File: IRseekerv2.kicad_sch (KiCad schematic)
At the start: 39 parts, among them J1 Conn_01x01_Female, J10 Conn_01x01_Female, J11 Conn_01x01_Female, J12 Conn_01x01_Female, J13 RESET, J14 COMM, J15 SEL_VOLTAGE, J16 G, J17 G, J18 G, J19 G, J2 Conn_01x01_Female, J20 COMM, J21 Conn_01x01_Female, J22 Conn_01x01_Female, J23 Conn_01x01_Female, J24 Conn_01x01_Female, J3 Conn_01x01_Female, J4 Conn_01x01_Female, J5 Conn_01x01_Female, J6 Conn_01x01_Female, J7 Conn_01x01_Female, J8 Conn_01x01_Female, J9 Conn_01x01_Female, U1 WeAct-STM32G431CoreBoard, U10 TSSP58038, U11 TSSP58038, U12 TSSP58038, U13 TSSP58038, U14 TSSP58038, U15 TSSP58038, U16 TSSP58038, U2 CD4072B, U4 CD4072B, U5 TSSP58038, U6 TSSP58038, U7 TSSP58038, U8 TSSP58038, U9 TSSP58038

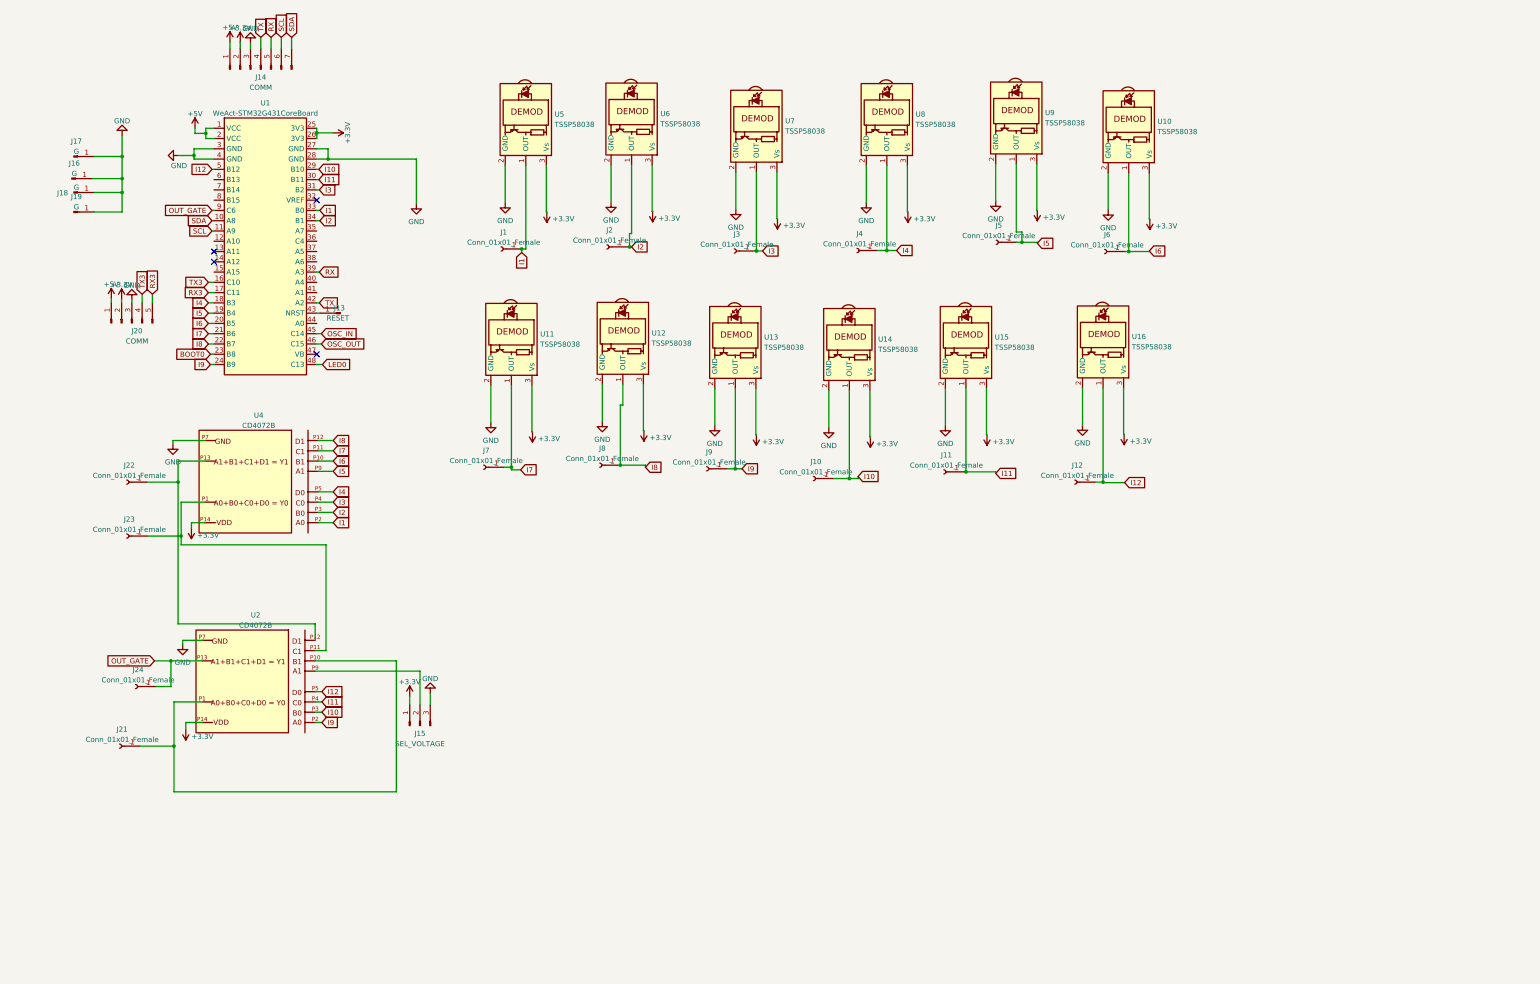
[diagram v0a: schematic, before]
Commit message: reworked to put STM32G431CBU6 on board
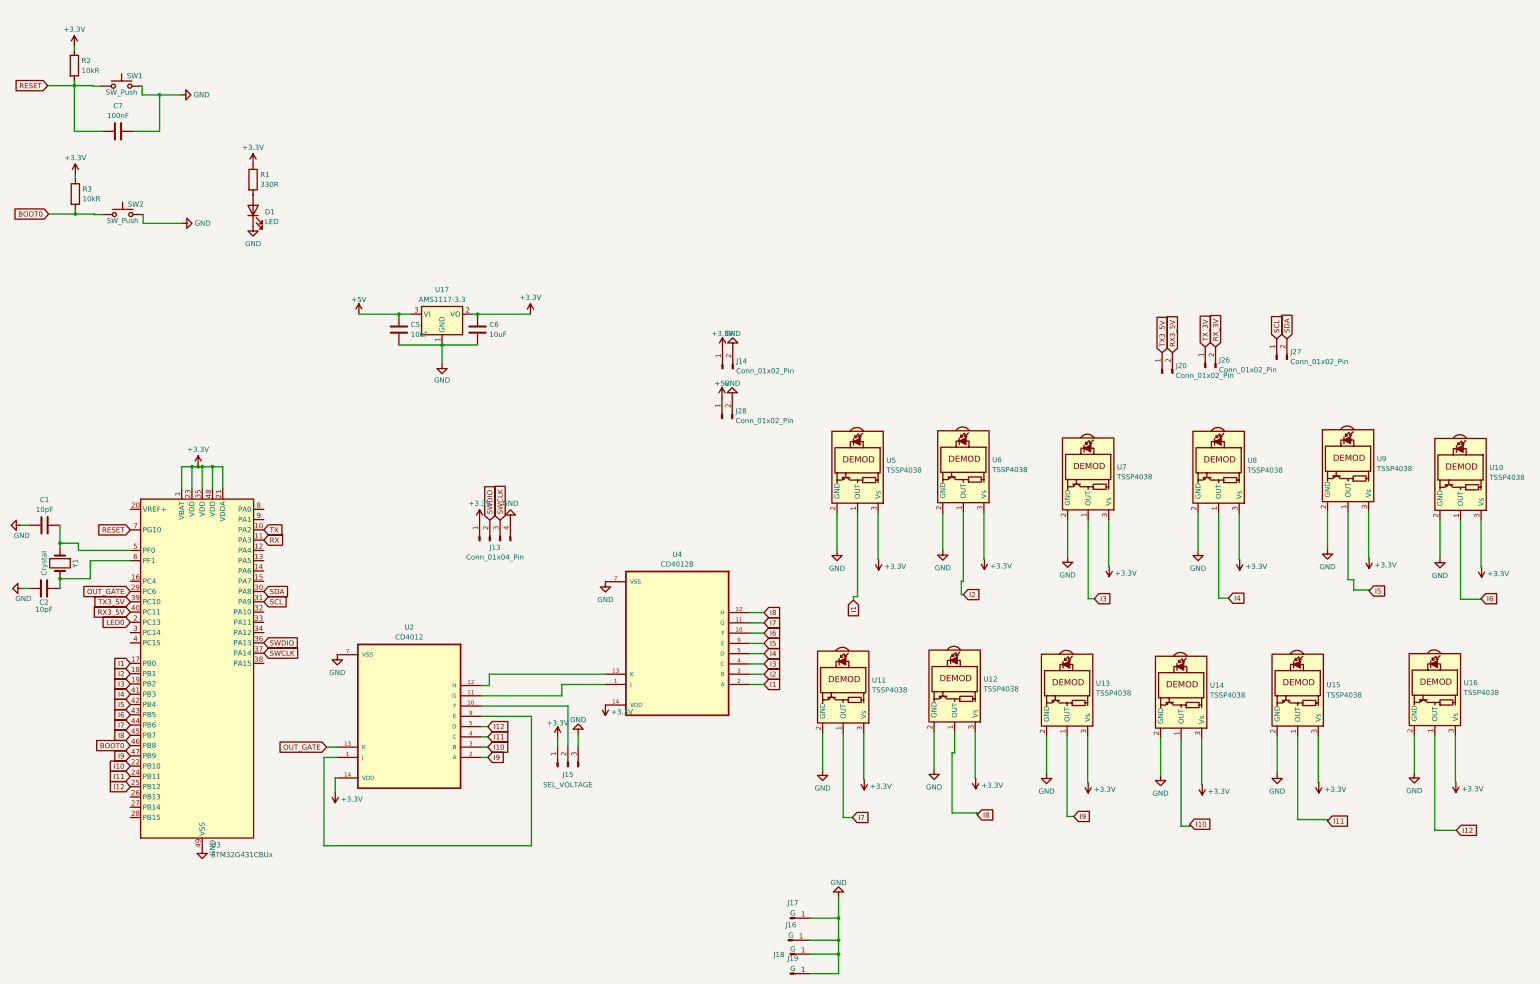
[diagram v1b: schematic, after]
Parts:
- removed J1, J10, J11, J12, J2, J21, J22, J23, J24, J3, J4, J5, J6, J7, J8, J9: Conn_01x01_Female, Connector_PinHeader_2.54mm:PinHeader_1x01_P2.54mm_Vertical, symbol Connector:Conn_01x01_Female
- removed J13: RESET, Connector_PinHeader_2.54mm:PinHeader_1x01_P2.54mm_Vertical, symbol Connector:Conn_01x01_Male
- removed J14: COMM, Connector_PinHeader_2.54mm:PinHeader_1x07_P2.54mm_Vertical, symbol Connector:Conn_01x07_Male
- removed J20: COMM, Connector_PinHeader_2.54mm:PinHeader_1x05_P2.54mm_Vertical, symbol Connector:Conn_01x05_Male
- removed U1: WeAct-STM32G431CoreBoard, bluepill:WeAct-STM32G431CoreBoard_MCU_Module, symbol bluepill:WeAct-STM32G431CoreBoard
- added C1, C2: 10pF, Capacitor_THT:C_Disc_D3.0mm_W1.6mm_P2.50mm, symbol Device:C
- added C5, C6: 10uF, Capacitor_THT:C_Disc_D3.0mm_W1.6mm_P2.50mm, symbol Device:C
- added C7: 100nF, Capacitor_THT:C_Disc_D3.0mm_W1.6mm_P2.50mm, symbol Device:C
- added D1: LED, LED_THT:LED_D3.0mm, symbol Device:LED
- added J13: Conn_01x04_Pin, Connector_PinHeader_2.54mm:PinHeader_1x04_P2.54mm_Vertical, symbol Connector:Conn_01x04_Pin
- added J14, J20, J26, J27, J28: Conn_01x02_Pin, Connector_PinHeader_2.54mm:PinHeader_1x02_P2.54mm_Vertical, symbol Connector:Conn_01x02_Pin
- added R1: 330R, Resistor_THT:R_Axial_DIN0204_L3.6mm_D1.6mm_P1.90mm_Vertical, symbol Device:R
- added R2, R3: 10kR, Resistor_THT:R_Axial_DIN0204_L3.6mm_D1.6mm_P1.90mm_Vertical, symbol Device:R
- added SW1, SW2: SW_Push, Button_Switch_THT:SW_PUSH_6mm, symbol Switch:SW_Push
- added U17: AMS1117-3.3, Package_TO_SOT_SMD:SOT-223-3_TabPin2, symbol Regulator_Linear:AMS1117-3.3
- added U3: STM32G431CBUx, Package_DFN_QFN:QFN-48-1EP_7x7mm_P0.5mm_EP5.6x5.6mm, symbol MCU_ST_STM32G4:STM32G431CBUx
- added Y1: Crystal, Crystal:Crystal_HC49-4H_Vertical, symbol Device:Crystal
- U10, U12, U14, U15, U5, U7: value TSSP58038 -> TSSP4038; footprint OptoDevice:Vishay_MINICAST-3Pin -> Vishay:Vishay_MINICAST-3Pin
- U11, U13, U16, U6, U8, U9: value TSSP58038 -> TSSP4038; footprint Library:Vishay_MINICAST-3PinMarek -> Vishay:Vishay_MINICAST-3Pin
- U2: value CD4072B -> CD4012; footprint CD4072B:DIP794W45P254L1969H508Q14 -> CD70xx:DIP794W45P254L1969H508Q14; symbol CD4072B:CD4072B -> CD4012:CD4012BE; Availability (none) -> In Stock; Check_prices (none) -> https://www.snapeda.com/parts/CD4012BE/Texas+Instruments/vi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; MF (none) -> Texas Instruments; MP (none) -> CD4012BE; Package (none) -> PDIP-14 Texas Instruments; Price (none) -> None; Purchase-URL (none) -> https://www.snapeda.com/api/url_track_click_mouser/?unipart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; SnapEDA_Link (none) -> https://www.snapeda.com/parts/CD4012BE/Texas+Instruments/vi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
- U4: value CD4072B -> CD4012B; footprint CD4072B:DIP794W45P254L1969H508Q14 -> CD70xx:DIP794W45P254L1969H508Q14; symbol CD4072B:CD4072B -> CD4012:CD4012BE; Availability (none) -> In Stock; Check_prices (none) -> https://www.snapeda.com/parts/CD4012BE/Texas+Instruments/vi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; MF (none) -> Texas Instruments; MP (none) -> CD4012BE; Package (none) -> PDIP-14 Texas Instruments; Price (none) -> None; Purchase-URL (none) -> https://www.snapeda.com/api/url_track_click_mouser/?unipart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; SnapEDA_Link (none) -> https://www.snapeda.com/parts/CD4012BE/Texas+Instruments/vi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
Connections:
- net +3.3V: now also U2.14 (VDD), U4.14 (VDD), C6.2, J13.1 (Pin_1), J14.1 (Pin_1), R1.1, R2.1, R3.1, U17.2 (VO), U3.1 (VBAT), U3.21 (VDDA), U3.23 (VDD), U3.35 (VDD), U3.48 (VDD); no longer U2.P14, U4.P14
- net +5V: now also C5.2, J28.1 (Pin_1), U17.3 (VI)
- net BOOT0: now also R3.2, SW2.1, U3.46 (PB8)
- net GND: now also U2.7 (VSS), U4.7 (VSS), C1.1, C2.1, C5.1, C6.1, C7.1, D1.1 (K), J13.4 (Pin_4), J14.2 (Pin_2), J28.2 (Pin_2), SW1.2, SW2.2, U17.1 (GND), U3.49 (VSS); no longer U2.P7, U4.P7
- net I1: now also U4.2 (A), U3.17 (PB0); no longer U4.P2
- net I10: now also U2.3 (B), U3.22 (PB10); no longer U2.P3
- net I11: now also U2.4 (C), U3.24 (PB11); no longer U2.P4
- net I12: now also U2.5 (D), U3.25 (PB12); no longer U2.P5
- net I2: now also U4.3 (B), U3.18 (PB1); no longer U4.P3
- net I3: now also U4.4 (C), U3.19 (PB2); no longer U4.P4
- net I4: now also U4.5 (D), U3.41 (PB3); no longer U4.P5
- net I5: now also U4.9 (E), U3.42 (PB4); no longer U4.P9
- net I6: now also U4.10 (F), U3.43 (PB5); no longer U4.P10
- net I7: now also U4.11 (G), U3.44 (PB6); no longer U4.P11
- net I8: now also U4.12 (H), U3.45 (PB7); no longer U4.P12
- net I9: now also U2.2 (A), U3.47 (PB9); no longer U2.P2
- net LED0: now also U3.2 (PC13)
- net OUT_GATE: now also U2.13 (K), U3.29 (PC6); no longer U2.P13
- net RX: now also U3.11 (PA3)
- net SCL: now also J27.1 (Pin_1), U3.31 (PA9)
- net SDA: now also J27.2 (Pin_2), U3.30 (PA8)
- net TX: now also U3.10 (PA2)
- net at J15.2 (Pin_2): now also U2.10 (F); no longer U2.P9
- new net: C2.2, U3.6 (PF1), Y1.2
- new net: C1.2, U3.5 (PF0), Y1.1
- new net: U2.11 (G), U4.1 (J)
- new net: U2.12 (H), U4.13 (K)
- new net: U2.1 (J), U2.9 (E)
- new net: D1.2 (A), R1.2
- new net RESET: C7.2, R2.2, SW1.1, U3.7 (PG10)
- new net RX3_5V: J20.2 (Pin_2), U3.40 (PC11)
- new net RX_3V: J26.2 (Pin_2)
- new net SWCLK: J13.3 (Pin_3), U3.37 (PA14)
- new net SWDIO: J13.2 (Pin_2), U3.36 (PA13)
- new net TX3_5V: J20.1 (Pin_1), U3.39 (PC10)
- new net TX_3V: J26.1 (Pin_1)
- no-connect marks 4 -> 0
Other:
- moved on the sheet: J15, J16, J17, J18, J19, U10, U11, U12, U13, U14, U15, U16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

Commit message: I2C pullup resistors
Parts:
- added R4, R5: 4.7kR, Resistor_THT:R_Axial_DIN0204_L3.6mm_D1.6mm_P2.54mm_Vertical, symbol Device:R
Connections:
- net +3.3V: now also R4.1, R5.2
- net SCL: now also R4.2
- net SDA: now also R5.1
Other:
- moved on the sheet: J27
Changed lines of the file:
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@@
   (junction (at 118.364 100.203) (diameter 0) (color 0 0 0 0)
   )
+  (junction (at 335.407 107.061) (diameter 0) (color 0 0 0 0)
+  )
   (junction (at 38.1 43.688) (diameter 0) (color 0 0 0 0)
   )
@@
   (junction (at 59.182 45.974) (diameter 0) (color 0 0 0 0)
   )
+  (junction (at 337.947 106.934) (diameter 0) (color 0 0 0 0)
+  )
   (junction (at 227.076 258.445) (diameter 0) (color 0 0 0 0)
   )
@@
     (stroke (width 0) (type default))
   )
+  (wire (pts (xy 335.407 107.061) (xy 335.407 107.823))
+    (stroke (width 0) (type default))
+  )
   (wire (pts (xy 43.053 75.565) (xy 44.958 75.565))
     (stroke (width 0) (type default))
@@
     (stroke (width 0) (type default))
   )
+  (wire (pts (xy 335.407 107.061) (xy 335.407 106.299))
+    (stroke (width 0) (type default))
+  )
   (wire (pts (xy 379.857 227.838) (xy 374.523 227.838))
     (stroke (width 0) (type default))
@@
     (stroke (width 0) (type default))
   )
+  (wire (pts (xy 337.947 106.299) (xy 337.947 106.934))
+    (stroke (width 0) (type default))
+  )
   (wire (pts (xy 236.855 160.909) (xy 236.982 160.909))
     (stroke (width 0) (type default))
@@
   )
   (wire (pts (xy 227.076 249.555) (xy 220.218 249.555))
+    (stroke (width 0) (type default))
+  )
+  (wire (pts (xy 337.947 106.934) (xy 337.947 107.823))
     (stroke (width 0) (type default))
   )
@@
   )
   (symbol (lib_id "Connector:Conn_01x02_Pin") (at 317.754 113.411 90) (unit 1)
-    (in_bom yes) (on_board yes) (dnp no) (fields_autoplaced)
+    (in_bom yes) (on_board yes) (dnp no)
     (property "Reference" "J26" (at 321.1322 111.5639 90)
       (effects (font (size 1.27 1.27)) (justify right))
     )
-    (property "Value" "Conn_01x02_Pin" (at 321.1322 113.9881 90)
+    (property "Value" "Conn_01x02_Pin" (at 312.801 117.475 90)
       (effects (font (size 1.27 1.27)) (justify right))
     )
@@
     )
   )
-  (symbol (lib_id "Connector:Conn_01x02_Pin") (at 335.407 111.379 90) (unit 1)
-    (in_bom yes) (on_board yes) (dnp no) (fields_autoplaced)
-    (property "Reference" "J27" (at 338.7852 109.5319 90)
+  (symbol (lib_id "Connector:Conn_01x02_Pin") (at 335.407 112.903 90) (unit 1)
+    (in_bom yes) (on_board yes) (dnp no) (fields_autoplaced)
+    (property "Reference" "J27" (at 338.7852 111.0559 90)
       (effects (font (size 1.27 1.27)) (justify right))
     )
-    (property "Value" "Conn_01x02_Pin" (at 338.7852 111.9561 90)
+    (property "Value" "Conn_01x02_Pin" (at 338.7852 113.4801 90)
       (effects (font (size 1.27 1.27)) (justify right))
     )
-    (property "Footprint" "Connector_PinHeader_2.54mm:PinHeader_1x02_P2.54mm_Vertical" (at 335.407 111.379 0)
-      (effects (font (size 1.27 1.27)) hide)
-    )
-    (property "Datasheet" "~" (at 335.407 111.379 0)
+    (property "Footprint" "Connector_PinHeader_2.54mm:PinHeader_1x02_P2.54mm_Vertical" (at 335.407 112.903 0)
+      (effects (font (size 1.27 1.27)) hide)
+    )
+    (property "Datasheet" "~" (at 335.407 112.903 0)
       (effects (font (size 1.27 1.27)) hide)
     )
@@
         (path "/c83ed66b-8f4f-4f32-bd83-eab9fc6ed48e"
           (reference "SW2") (unit 1)
+        )
+      )
+    )
+  )
+  (symbol (lib_id "Device:R") (at 341.757 106.934 90) (unit 1)
+    (in_bom yes) (on_board yes) (dnp no) (fields_autoplaced)
+    (property "Reference" "R5" (at 341.757 101.7737 90)
+      (effects (font (size 1.27 1.27)))
+    )
+    (property "Value" "4.7kR" (at 341.757 104.1979 90)
+      (effects (font (size 1.27 1.27)))
+    )
+    (property "Footprint" "Resistor_THT:R_Axial_DIN0204_L3.6mm_D1.6mm_P2.54mm_Vertical" (at 341.757 108.712 90)
+      (effects (font (size 1.27 1.27)) hide)
+    )
+    (property "Datasheet" "~" (at 341.757 106.934 0)
+      (effects (font (size 1.27 1.27)) hide)
+    )
+    (pin "1")
+    (pin "2")
+    (instances
+      (project "IRseekerv2"
+        (path "/c83ed66b-8f4f-4f32-bd83-eab9fc6ed48e"
+          (reference "R5") (unit 1)
         )
       )
@@
         (path "/c83ed66b-8f4f-4f32-bd83-eab9fc6ed48e"
           (reference "#PWR011") (unit 1)
+        )
+      )
+    )
+  )
+  (symbol (lib_id "power:+3.3V") (at 327.787 107.061 0) (unit 1)
+    (in_bom yes) (on_board yes) (dnp no) (fields_autoplaced)
+    (property "Reference" "#PWR024" (at 327.787 110.871 0)
+      (effects (font (size 1.27 1.27)) hide)
+    )
+    (property "Value" "+3.3V" (at 327.787 102.9279 0)
+      (effects (font (size 1.27 1.27)))
+    )
+    (property "Footprint" "" (at 327.787 107.061 0)
+      (effects (font (size 1.27 1.27)) hide)
+    )
+    (property "Datasheet" "" (at 327.787 107.061 0)
+      (effects (font (size 1.27 1.27)) hide)
+    )
+    (pin "1")
+    (instances
+      (project "IRseekerv2"
+        (path "/c83ed66b-8f4f-4f32-bd83-eab9fc6ed48e"
+          (reference "#PWR024") (unit 1)
         )
       )
@@
     )
   )
+  (symbol (lib_id "power:+3.3V") (at 345.567 106.934 0) (unit 1)
+    (in_bom yes) (on_board yes) (dnp no) (fields_autoplaced)
+    (property "Reference" "#PWR025" (at 345.567 110.744 0)
+      (effects (font (size 1.27 1.27)) hide)
+    )
+    (property "Value" "+3.3V" (at 345.567 102.8009 0)
+      (effects (font (size 1.27 1.27)))
+    )
+    (property "Footprint" "" (at 345.567 106.934 0)
+      (effects (font (size 1.27 1.27)) hide)
+    )
+    (property "Datasheet" "" (at 345.567 106.934 0)
+      (effects (font (size 1.27 1.27)) hide)
+    )
+    (pin "1")
+    (instances
+      (project "IRseekerv2"
+        (path "/c83ed66b-8f4f-4f32-bd83-eab9fc6ed48e"
+          (reference "#PWR025") (unit 1)
+        )
+      )
+    )
+  )
   (symbol (lib_id "Device:C") (at 48.895 54.991 270) (unit 1)
     (in_bom yes) (on_board yes) (dnp no) (fields_autoplaced)
@@
         )
       )
+    )
+  )
+  (symbol (lib_id "Device:R") (at 331.597 107.061 90) (unit 1)
+    (in_bom yes) (on_board yes) (dnp no) (fields_autoplaced)
+    (property "Reference" "R4" (at 331.597 101.9007 90)
+      (effects (font (size 1.27 1.27)))
+    )
+    (property "Value" "4.7kR" (at 331.597 104.3249 90)
+      (effects (font (size 1.27 1.27)))
+    )
+    (property "Footprint" "Resistor_THT:R_Axial_DIN0204_L3.6mm_D1.6mm_P2.54mm_Vertical" (at 331.597 108.839 90)
+      (effects (font (size 1.27 1.27)) hide)
+    )
+    (property "Datasheet" "~" (at 331.597 107.061 0)
+      (effects (font (size 1.27 1.27)) hide)
+    )
+    (pin "1")
+    (pin "2")
+    (instances
+      (project "IRseekerv2"
+        (path "/c83ed66b-8f4f-4f32-bd83-eab9fc6ed48e"
+          (reference "R4") (unit 1)
+        )
+      )
